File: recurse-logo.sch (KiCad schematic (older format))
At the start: 18 parts, among them Q1 MMBT3904, Q2 MMBT3904

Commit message: Updates and change to relative paths
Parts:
- D1, D2, D3, D4, D5, D6, D7: footprint Inductor_SMD:L_0603_1608Metric_Pad1.05x0.95mm_HandSolder -> LED_THT:LED_Rectangular_W5.0mm_H5.0mm-top-left
- R1, R2, R3, R4, R5, R6: footprint Resistor_SMD:R_0201_0603Metric -> Resistor_SMD:R_2010_5025Metric_Pad1.52x2.65mm_HandSolder
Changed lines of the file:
@@
 F 0 "R2" H 3730 2804 50  0000 R CNN
 F 1 "10K" H 3730 2895 50  0000 R CNN
-F 2 "Resistor_SMD:R_0201_0603Metric" V 3730 2850 50  0001 C CNN
+F 2 "Resistor_SMD:R_2010_5025Metric_Pad1.52x2.65mm_HandSolder" V 3730 2850 50  0001 C CNN
 F 3 "~" H 3800 2850 50  0001 C CNN
 	1    3800 2850
@@
 F 0 "R3" H 4030 2804 50  0000 R CNN
 F 1 "10K" H 4030 2895 50  0000 R CNN
-F 2 "Resistor_SMD:R_0201_0603Metric" V 4030 2850 50  0001 C CNN
+F 2 "Resistor_SMD:R_2010_5025Metric_Pad1.52x2.65mm_HandSolder" V 4030 2850 50  0001 C CNN
 F 3 "~" H 4100 2850 50  0001 C CNN
 	1    4100 2850
@@
 F 0 "R4" H 5570 2896 50  0000 L CNN
 F 1 "10K" H 5570 2805 50  0000 L CNN
-F 2 "Resistor_SMD:R_0201_0603Metric" V 5430 2850 50  0001 C CNN
+F 2 "Resistor_SMD:R_2010_5025Metric_Pad1.52x2.65mm_HandSolder" V 5430 2850 50  0001 C CNN
 F 3 "~" H 5500 2850 50  0001 C CNN
 	1    5500 2850
@@
 F 0 "R5" H 5870 2896 50  0000 L CNN
 F 1 "10K" H 5870 2805 50  0000 L CNN
-F 2 "Resistor_SMD:R_0201_0603Metric" V 5730 2850 50  0001 C CNN
+F 2 "Resistor_SMD:R_2010_5025Metric_Pad1.52x2.65mm_HandSolder" V 5730 2850 50  0001 C CNN
 F 3 "~" H 5800 2850 50  0001 C CNN
 	1    5800 2850
@@
 F 0 "D4" V 6838 2733 50  0000 R CNN
 F 1 "LED" V 6747 2733 50  0000 R CNN
-F 2 "Inductor_SMD:L_0603_1608Metric_Pad1.05x0.95mm_HandSolder" H 6800 2850 50  0001 C CNN
+F 2 "LED_THT:LED_Rectangular_W5.0mm_H5.0mm-top-left" H 6800 2850 50  0001 C CNN
 F 3 "~" H 6800 2850 50  0001 C CNN
 	1    6800 2850
@@
 F 0 "D1" V 2738 3033 50  0000 R CNN
 F 1 "LED" V 2647 3033 50  0000 R CNN
-F 2 "Inductor_SMD:L_0603_1608Metric_Pad1.05x0.95mm_HandSolder" H 2700 3150 50  0001 C CNN
+F 2 "LED_THT:LED_Rectangular_W5.0mm_H5.0mm-top-left" H 2700 3150 50  0001 C CNN
 F 3 "~" H 2700 3150 50  0001 C CNN
 	1    2700 3150
@@
 F 0 "R6" V 5793 3200 50  0000 C CNN
 F 1 "220" V 5884 3200 50  0000 C CNN
-F 2 "Resistor_SMD:R_0201_0603Metric" V 5930 3200 50  0001 C CNN
+F 2 "Resistor_SMD:R_2010_5025Metric_Pad1.52x2.65mm_HandSolder" V 5930 3200 50  0001 C CNN
 F 3 "~" H 6000 3200 50  0001 C CNN
 	1    6000 3200
@@
 F 0 "R1" V 3393 3200 50  0000 C CNN
 F 1 "220" V 3484 3200 50  0000 C CNN
-F 2 "Resistor_SMD:R_0201_0603Metric" V 3530 3200 50  0001 C CNN
+F 2 "Resistor_SMD:R_2010_5025Metric_Pad1.52x2.65mm_HandSolder" V 3530 3200 50  0001 C CNN
 F 3 "~" H 3600 3200 50  0001 C CNN
 	1    3600 3200
@@
 F 0 "D5" V 6838 3033 50  0000 R CNN
 F 1 "LED" V 6747 3033 50  0000 R CNN
-F 2 "Inductor_SMD:L_0603_1608Metric_Pad1.05x0.95mm_HandSolder" H 6800 3150 50  0001 C CNN
+F 2 "LED_THT:LED_Rectangular_W5.0mm_H5.0mm-top-left" H 6800 3150 50  0001 C CNN
 F 3 "~" H 6800 3150 50  0001 C CNN
 	1    6800 3150
@@
 F 0 "D6" V 6838 3333 50  0000 R CNN
 F 1 "LED" V 6747 3333 50  0000 R CNN
-F 2 "Inductor_SMD:L_0603_1608Metric_Pad1.05x0.95mm_HandSolder" H 6800 3450 50  0001 C CNN
+F 2 "LED_THT:LED_Rectangular_W5.0mm_H5.0mm-top-left" H 6800 3450 50  0001 C CNN
 F 3 "~" H 6800 3450 50  0001 C CNN
 	1    6800 3450
@@
 F 0 "D7" V 6838 3633 50  0000 R CNN
 F 1 "LED" V 6747 3633 50  0000 R CNN
-F 2 "Inductor_SMD:L_0603_1608Metric_Pad1.05x0.95mm_HandSolder" H 6800 3750 50  0001 C CNN
+F 2 "LED_THT:LED_Rectangular_W5.0mm_H5.0mm-top-left" H 6800 3750 50  0001 C CNN
 F 3 "~" H 6800 3750 50  0001 C CNN
 	1    6800 3750
@@
 F 0 "D2" V 2738 3333 50  0000 R CNN
 F 1 "LED" V 2647 3333 50  0000 R CNN
-F 2 "Inductor_SMD:L_0603_1608Metric_Pad1.05x0.95mm_HandSolder" H 2700 3450 50  0001 C CNN
+F 2 "LED_THT:LED_Rectangular_W5.0mm_H5.0mm-top-left" H 2700 3450 50  0001 C CNN
 F 3 "~" H 2700 3450 50  0001 C CNN
 	1    2700 3450
@@
 F 0 "D3" V 2738 3633 50  0000 R CNN
 F 1 "LED" V 2647 3633 50  0000 R CNN
-F 2 "Inductor_SMD:L_0603_1608Metric_Pad1.05x0.95mm_HandSolder" H 2700 3750 50  0001 C CNN
+F 2 "LED_THT:LED_Rectangular_W5.0mm_H5.0mm-top-left" H 2700 3750 50  0001 C CNN
 F 3 "~" H 2700 3750 50  0001 C CNN
 	1    2700 3750

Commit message: Wired it up! needs finishing touches
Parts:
- C2: value 100mF -> 100uF
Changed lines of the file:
@@
 EESchema Schematic File Version 4
-EELAYER 26 0
+LIBS:recurse-logo-cache
+EELAYER 29 0
 EELAYER END
 $Descr A4 11693 8268
@@
 Data
 89 50 4E 47 0D 0A 1A 0A 00 00 00 0D 49 48 44 52 00 00 01 E3 00 00 01 02 08 03 00 00 00 FA B1 4F
-2D 00 00 00 03 73 42 49 54 08 08 08 DB E1 4F E0 00 00 03 00 50 4C 54 45 FF 00 FF FF FF E2 9D 48
+2D 00 00 00 03 73 42 49 54 08 08 08 DB E1 4F E0 00 00 03 00 50 4C 54 45 01 00 00 FF FF E2 9D 48
 00 00 00 00 48 9D E2 FF FF BE 75 00 00 E2 9D 48 00 00 75 BE FF FF BE 75 00 00 75 BE 75 BE FF FF
 E2 9D 48 00 48 9D E2 FF FF BE 75 75 00 75 00 48 9D E2 FF FF 9D 75 00 9D E2 E2 75 00 48 48 00 75
@@
 0C 40 44 44 79 7D 89 75 48 9D FF E6 AA AE 3C 34 9D 3C 34 9D 89 C6 F2 AA 61 C2 CA FF FF FF C6 C2
 3C 61 D2 E6 FF C2 3C 34 9D 65 AA F2 FF FF 9D 3C 61 FF CA 85 E2 89 34 AE 3C 61 9D 3C 85 D2 65 34
-AE 3C 85 D2 AA 85 AE AA E2 9D 89 85 E2 FF C6 E2 AA 61 AE 89 85 AE AA AA 8F C0 F1 43 00 00 00 01
+AE 3C 85 D2 AA 85 AE AA E2 9D 89 85 E2 FF C6 E2 AA 61 AE 89 85 AE AA AA 4B 59 C7 76 00 00 00 01
 74 52 4E 53 00 40 E6 D8 66 00 00 19 E2 49 44 41 54 78 9C ED 9D 09 7C 1D C5 7D C7 9F BC 96 65 84
 85 5D BB 85 48 4F D7 93 9F 9E 04 3A 9F 2E AC 27 CB 92 2A 61 BB 7E 3C 09 92 34 B8 BC D4 98 CB 2E
@@
 P 5100 3200
 F 0 "C2" V 5355 3200 50  0000 C CNN
-F 1 "100mF" V 5264 3200 50  0000 C CNN
+F 1 "100uF" V 5264 3200 50  0000 C CNN
 F 2 "Capacitor_SMD:CP_Elec_6.3x5.4_Nichicon" H 5138 3050 50  0001 C CNN
 F 3 "~" H 5100 3200 50  0001 C CNN

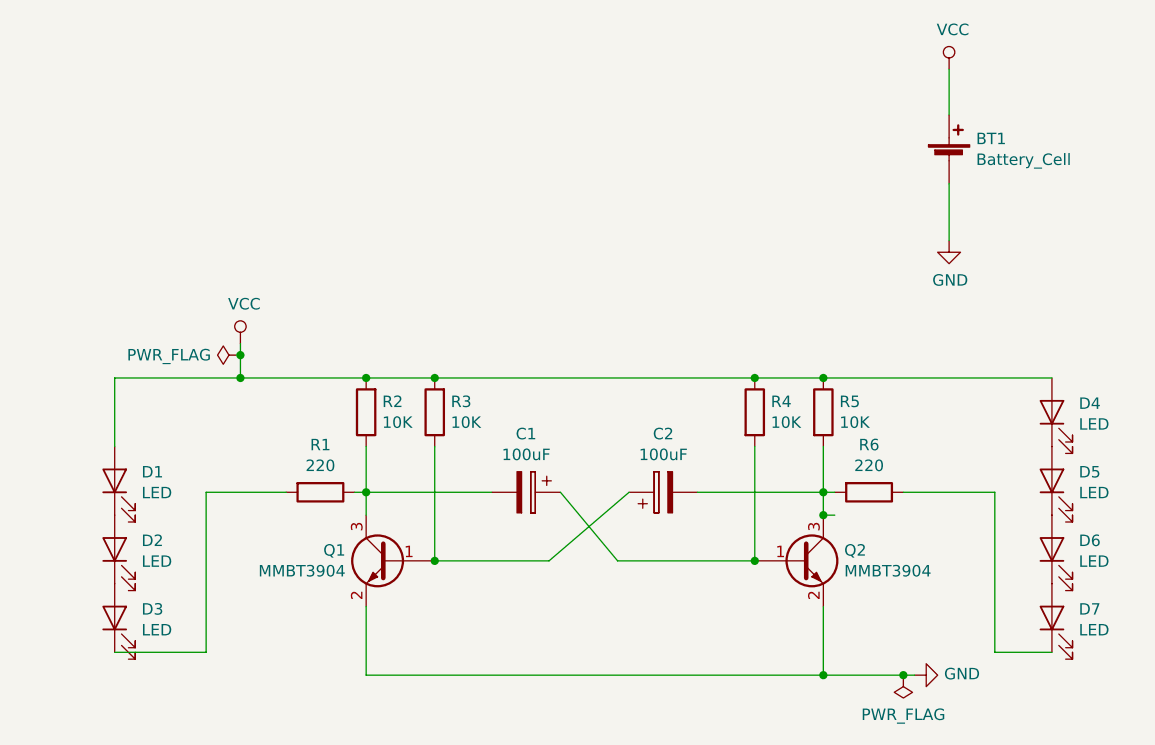
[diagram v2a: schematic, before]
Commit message: put LEDs in Parallel and get rid of the resistor\n also add the switch- but the assigned footprint isn't right
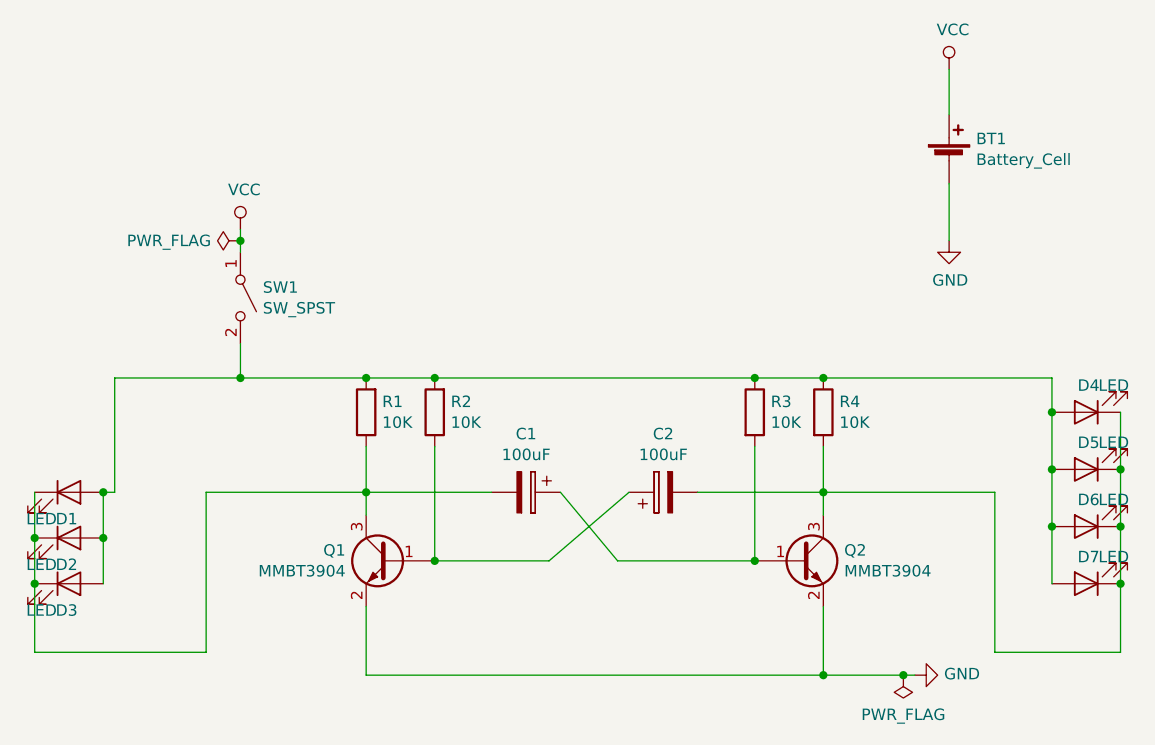
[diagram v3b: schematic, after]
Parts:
- removed R1, R6: 220, Resistor_SMD:R_2010_5025Metric_Pad1.52x2.65mm_HandSolder, symbol Device:R
- added SW1: SW_SPST, symbol Switch:SW_SPST
- renumbered R2 to R1, R3 to R2, R4 to R3, R5 to R4
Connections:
- wire segments 37 -> 49
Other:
- moved on the sheet: D1, D2, D3, D4, D5, D6, D7
